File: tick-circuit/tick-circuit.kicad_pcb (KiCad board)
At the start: 2 copper layers, 48.3 x 33 mm, 14 parts, among them J1 Power, J2 50/60Hz, U1 74HCT4060, U2 74HCT73, X1 3.93216 MHz

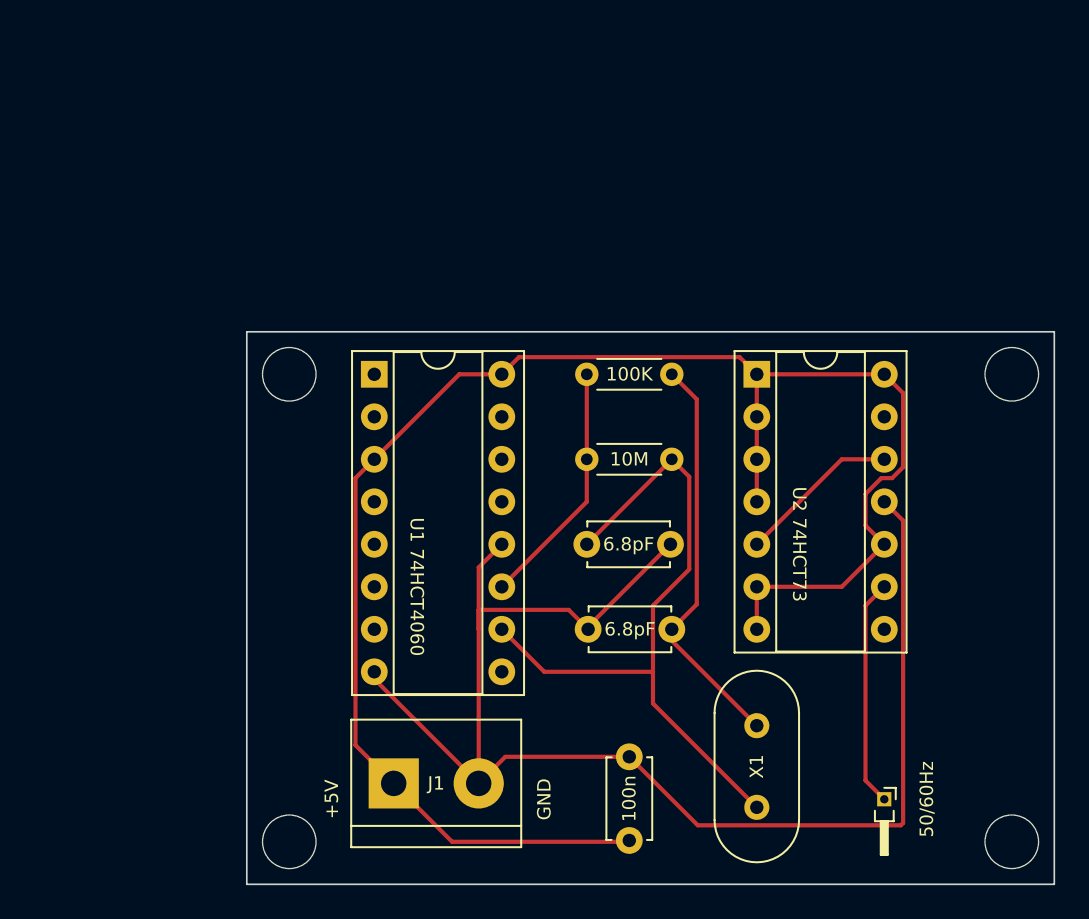
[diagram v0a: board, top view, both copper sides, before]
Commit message: Use both layers, add ground fills
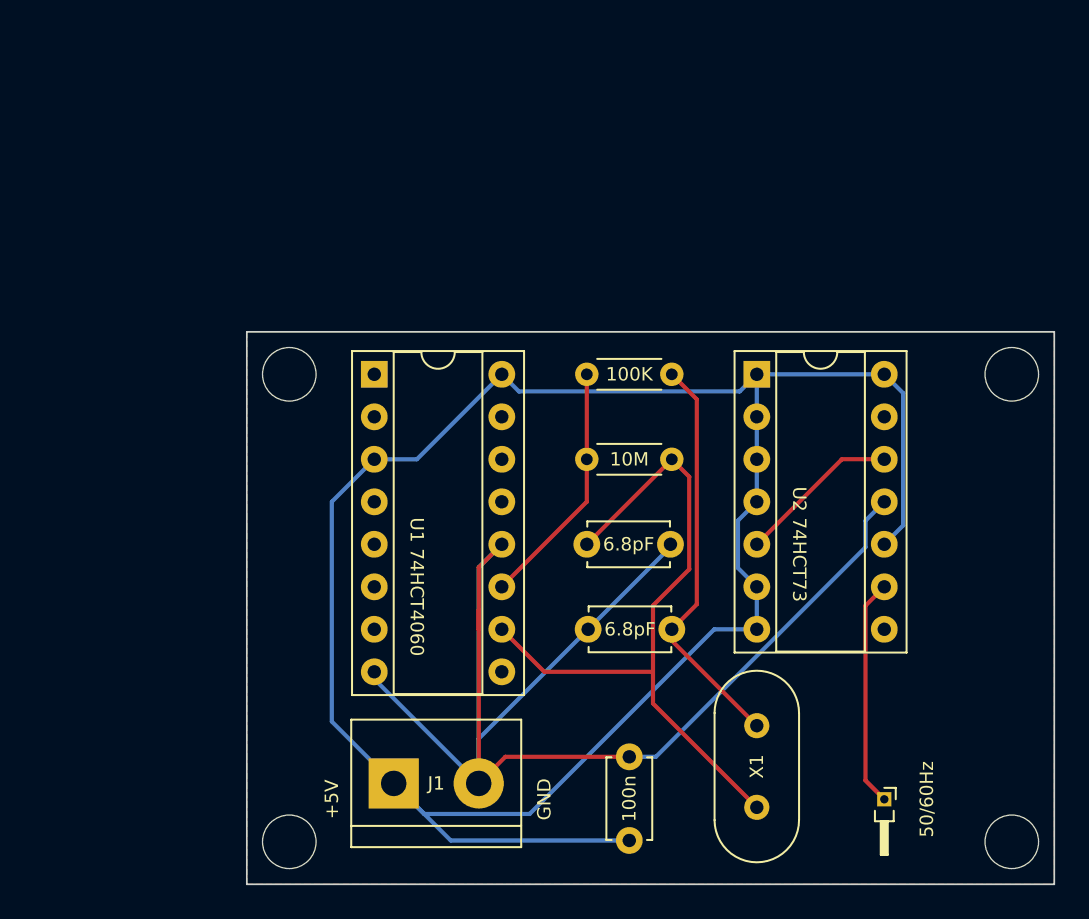
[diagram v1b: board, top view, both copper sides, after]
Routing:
- net +5V: track 101.0 -> 125.2 mm
- net GND: track 86.9 -> 91.3 mm
- added copper zone on B.Cu, net GND
- added copper zone on F.Cu, net GND
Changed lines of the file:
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@@
   (segment (start 50.8 38.1) (end 51.845 39.145) (width 0.25) (layer "F.Cu") (net 1))
   (segment (start 55.88 58.42) (end 55.88 58.9) (width 0.25) (layer "F.Cu") (net 1))
-  (segment (start 45.8 48.1) (end 45.8 48.26) (width 0.25) (layer "F.Cu") (net 2))
   (segment (start 39.26 47.1) (end 39.26 48.26) (width 0.25) (layer "F.Cu") (net 2))
-  (segment (start 33.02 51.23) (end 33.02 50.8) (width 0.25) (layer "F.Cu") (net 2))
   (segment (start 39.26 48.26) (end 39.26 44.56) (width 0.25) (layer "F.Cu") (net 2))
-  (segment (start 64.485 59.975) (end 52.355 59.975) (width 0.25) (layer "F.Cu") (net 2))
   (segment (start 39.26 57.47) (end 39.26 48.26) (width 0.25) (layer "F.Cu") (net 2))
-  (segment (start 63.5 40.64) (end 64.625 41.765) (width 0.25) (layer "F.Cu") (net 2))
   (segment (start 40.85 55.88) (end 39.26 57.47) (width 0.25) (layer "F.Cu") (net 2))
   (segment (start 48.26 55.88) (end 40.85 55.88) (width 0.25) (layer "F.Cu") (net 2))
-  (segment (start 44.64 47.1) (end 39.26 47.1) (width 0.25) (layer "F.Cu") (net 2))
-  (segment (start 50.72 43.18) (end 45.8 48.1) (width 0.25) (layer "F.Cu") (net 2))
   (segment (start 39.26 44.56) (end 40.64 43.18) (width 0.25) (layer "F.Cu") (net 2))
-  (segment (start 45.8 48.26) (end 44.64 47.1) (width 0.25) (layer "F.Cu") (net 2))
-  (segment (start 64.625 41.765) (end 64.625 59.835) (width 0.25) (layer "F.Cu") (net 2))
-  (segment (start 64.625 59.835) (end 64.485 59.975) (width 0.25) (layer "F.Cu") (net 2))
-  (segment (start 52.355 59.975) (end 48.26 55.88) (width 0.25) (layer "F.Cu") (net 2))
-  (segment (start 39.26 57.47) (end 33.02 51.23) (width 0.25) (layer "F.Cu") (net 2))
+  (segment (start 39.26 44.56) (end 40.64 43.18) (width 0.25) (layer "B.Cu") (net 2))
+  (segment (start 39.26 57.47) (end 39.26 44.56) (width 0.25) (layer "B.Cu") (net 2))
+  (segment (start 39.26 57.47) (end 33.02 51.23) (width 0.25) (layer "B.Cu") (net 2))
+  (segment (start 33.02 51.23) (end 33.02 50.8) (width 0.25) (layer "B.Cu") (net 2))
+  (segment (start 48.26 55.88) (end 49.850991 55.88) (width 0.25) (layer "B.Cu") (net 2))
+  (segment (start 49.850991 55.88) (end 62.375 43.355991) (width 0.25) (layer "B.Cu") (net 2))
+  (segment (start 39.26 54.8) (end 45.8 48.26) (width 0.25) (layer "B.Cu") (net 2))
+  (segment (start 45.8 48.26) (end 50.72 43.34) (width 0.25) (layer "B.Cu") (net 2))
+  (segment (start 62.375 41.765) (end 63.5 40.64) (width 0.25) (layer "B.Cu") (net 2))
+  (segment (start 62.375 43.355991) (end 62.375 41.765) (width 0.25) (layer "B.Cu") (net 2))
+  (segment (start 50.72 43.34) (end 50.72 43.18) (width 0.25) (layer "B.Cu") (net 2))
+  (segment (start 39.26 57.47) (end 39.26 54.8) (width 0.25) (layer "B.Cu") (net 2))
   (segment (start 55.88 54.02) (end 50.8 48.94) (width 0.25) (layer "F.Cu") (net 3))
   (segment (start 50.8 48.94) (end 50.8 48.26) (width 0.25) (layer "F.Cu") (net 3))
@@
   (segment (start 50.8 33.02) (end 52.295 34.515) (width 0.25) (layer "F.Cu") (net 3))
   (segment (start 52.295 34.515) (end 52.295 46.765) (width 0.25) (layer "F.Cu") (net 3))
-  (segment (start 34.18 57.47) (end 31.895 55.185) (width 0.25) (layer "F.Cu") (net 4))
-  (segment (start 31.895 55.185) (end 31.895 39.225) (width 0.25) (layer "F.Cu") (net 4))
-  (segment (start 55.88 33.02) (end 55.88 35.56) (width 0.25) (layer "F.Cu") (net 4))
-  (segment (start 34.18 57.47) (end 37.67 60.96) (width 0.25) (layer "F.Cu") (net 4))
-  (segment (start 31.895 39.225) (end 33.02 38.1) (width 0.25) (layer "F.Cu") (net 4))
-  (segment (start 62.375 40.174009) (end 63.324009 39.225) (width 0.25) (layer "F.Cu") (net 4))
-  (segment (start 63.324009 39.225) (end 63.965991 39.225) (width 0.25) (layer "F.Cu") (net 4))
-  (segment (start 38.1 33.02) (end 40.64 33.02) (width 0.25) (layer "F.Cu") (net 4))
-  (segment (start 55.88 35.56) (end 55.88 38.1) (width 0.25) (layer "F.Cu") (net 4))
-  (segment (start 63.965991 39.225) (end 64.625 38.565991) (width 0.25) (layer "F.Cu") (net 4))
-  (segment (start 55.88 33.02) (end 63.5 33.02) (width 0.25) (layer "F.Cu") (net 4))
-  (segment (start 37.67 60.96) (end 48.26 60.96) (width 0.25) (layer "F.Cu") (net 4))
-  (segment (start 33.02 38.1) (end 38.1 33.02) (width 0.25) (layer "F.Cu") (net 4))
-  (segment (start 60.96 45.72) (end 63.5 43.18) (width 0.25) (layer "F.Cu") (net 4))
-  (segment (start 55.88 45.72) (end 60.96 45.72) (width 0.25) (layer "F.Cu") (net 4))
-  (segment (start 54.855 31.995) (end 55.88 33.02) (width 0.25) (layer "F.Cu") (net 4))
-  (segment (start 64.625 38.565991) (end 64.625 34.145) (width 0.25) (layer "F.Cu") (net 4))
-  (segment (start 63.5 43.18) (end 62.375 42.055) (width 0.25) (layer "F.Cu") (net 4))
-  (segment (start 40.64 33.02) (end 41.665 31.995) (width 0.25) (layer "F.Cu") (net 4))
-  (segment (start 55.88 38.1) (end 55.88 40.64) (width 0.25) (layer "F.Cu") (net 4))
-  (segment (start 62.375 42.055) (end 62.375 40.174009) (width 0.25) (layer "F.Cu") (net 4))
-  (segment (start 41.665 31.995) (end 54.855 31.995) (width 0.25) (layer "F.Cu") (net 4))
-  (segment (start 63.5 33.02) (end 64.625 34.145) (width 0.25) (layer "F.Cu") (net 4))
-  (segment (start 55.88 45.72) (end 55.88 48.26) (width 0.25) (layer "F.Cu") (net 4))
+  (segment (start 37.59 60.88) (end 34.18 57.47) (width 0.25) (layer "B.Cu") (net 4))
+  (segment (start 63.5 43.18) (end 64.625 42.055) (width 0.25) (layer "B.Cu") (net 4))
+  (segment (start 54.855 34.045) (end 41.665 34.045) (width 0.25) (layer "B.Cu") (net 4))
+  (segment (start 33.02 38.1) (end 30.48 40.64) (width 0.25) (layer "B.Cu") (net 4))
+  (segment (start 64.625 34.145) (end 63.5 33.02) (width 0.25) (layer "B.Cu") (net 4))
+  (segment (start 30.48 40.64) (end 30.48 53.77) (width 0.25) (layer "B.Cu") (net 4))
+  (segment (start 54.755 41.765) (end 55.88 40.64) (width 0.25) (layer "B.Cu") (net 4))
+  (segment (start 48.26 60.88) (end 37.59 60.88) (width 0.25) (layer "B.Cu") (net 4))
+  (segment (start 55.88 33.02) (end 63.5 33.02) (width 0.25) (layer "B.Cu") (net 4))
+  (segment (start 55.88 33.02) (end 55.88 35.56) (width 0.25) (layer "B.Cu") (net 4))
+  (segment (start 30.48 53.77) (end 34.18 57.47) (width 0.25) (layer "B.Cu") (net 4))
+  (segment (start 55.88 38.1) (end 55.88 40.64) (width 0.25) (layer "B.Cu") (net 4))
+  (segment (start 33.02 38.1) (end 35.56 38.1) (width 0.25) (layer "B.Cu") (net 4))
+  (segment (start 41.665 34.045) (end 40.64 33.02) (width 0.25) (layer "B.Cu") (net 4))
+  (segment (start 53.34 48.26) (end 55.88 48.26) (width 0.25) (layer "B.Cu") (net 4))
+  (segment (start 36.005 59.295) (end 42.305 59.295) (width 0.25) (layer "B.Cu") (net 4))
+  (segment (start 54.755 44.595) (end 54.755 41.765) (width 0.25) (layer "B.Cu") (net 4))
+  (segment (start 55.88 35.56) (end 55.88 38.1) (width 0.25) (layer "B.Cu") (net 4))
+  (segment (start 35.56 38.1) (end 40.64 33.02) (width 0.25) (layer "B.Cu") (net 4))
+  (segment (start 55.88 33.02) (end 54.855 34.045) (width 0.25) (layer "B.Cu") (net 4))
+  (segment (start 55.88 45.72) (end 54.755 44.595) (width 0.25) (layer "B.Cu") (net 4))
+  (segment (start 55.88 48.26) (end 55.88 45.72) (width 0.25) (layer "B.Cu") (net 4))
+  (segment (start 34.18 57.47) (end 36.005 59.295) (width 0.25) (layer "B.Cu") (net 4))
+  (segment (start 42.305 59.295) (end 53.34 48.26) (width 0.25) (layer "B.Cu") (net 4))
+  (segment (start 64.625 42.055) (end 64.625 34.145) (width 0.25) (layer "B.Cu") (net 4))
   (segment (start 62.375 46.845) (end 63.5 45.72) (width 0.25) (layer "F.Cu") (net 5))
   (segment (start 62.375 57.295) (end 62.375 46.845) (width 0.25) (layer "F.Cu") (net 5))
@@
   (segment (start 60.96 38.1) (end 55.88 43.18) (width 0.25) (layer "F.Cu") (net 17))
   (segment (start 63.5 38.1) (end 60.96 38.1) (width 0.25) (layer "F.Cu") (net 17))
+  (zone (net 2) (net_name "GND") (layer "F.Cu") (hatch edge 0.5)
+    (connect_pads (clearance 0.5))
+    (min_thickness 0.25) (filled_areas_thickness no)
+    (fill yes (thermal_gap 0.5) (thermal_bridge_width 0.5))
+    (polygon
+      (pts
+        (xy 25.4 30.48)
+        (xy 25.4 63.5)
+        (xy 73.66 63.5)
+        (xy 73.66 30.48)
+      )
+    )
+  )
+  (zone (net 2) (net_name "GND") (layer "B.Cu") (hatch edge 0.5)
+    (priority 1)
+    (connect_pads (clearance 0.5))
+    (min_thickness 0.25) (filled_areas_thickness no)
+    (fill yes (thermal_gap 0.5) (thermal_bridge_width 0.5))
+    (polygon
+      (pts
+        (xy 25.4 30.48)
+        (xy 73.66 30.48)
+        (xy 73.66 63.5)
+        (xy 25.4 63.5)
+      )
+    )
+  )
 )

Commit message: No need for ground routing if it is all ground
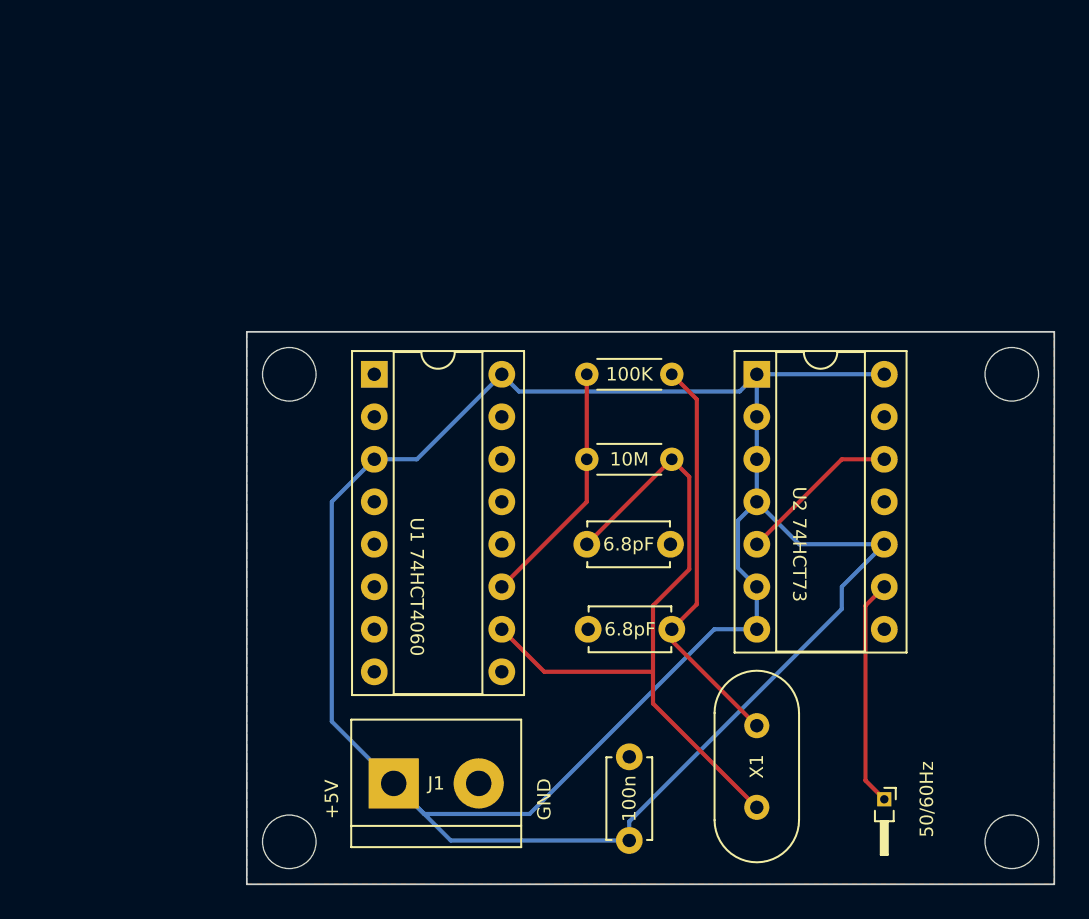
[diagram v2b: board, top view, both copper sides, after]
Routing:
- net GND: track 91.3 -> 0.59 mm
- net +5V: track 125.2 -> 146.8 mm
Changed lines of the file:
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@@
   (segment (start 50.8 38.1) (end 51.845 39.145) (width 0.25) (layer "F.Cu") (net 1))
   (segment (start 55.88 58.42) (end 55.88 58.9) (width 0.25) (layer "F.Cu") (net 1))
-  (segment (start 39.26 47.1) (end 39.26 48.26) (width 0.25) (layer "F.Cu") (net 2))
-  (segment (start 39.26 48.26) (end 39.26 44.56) (width 0.25) (layer "F.Cu") (net 2))
-  (segment (start 39.26 57.47) (end 39.26 48.26) (width 0.25) (layer "F.Cu") (net 2))
-  (segment (start 40.85 55.88) (end 39.26 57.47) (width 0.25) (layer "F.Cu") (net 2))
-  (segment (start 48.26 55.88) (end 40.85 55.88) (width 0.25) (layer "F.Cu") (net 2))
-  (segment (start 39.26 44.56) (end 40.64 43.18) (width 0.25) (layer "F.Cu") (net 2))
-  (segment (start 39.26 44.56) (end 40.64 43.18) (width 0.25) (layer "B.Cu") (net 2))
-  (segment (start 39.26 57.47) (end 39.26 44.56) (width 0.25) (layer "B.Cu") (net 2))
-  (segment (start 39.26 57.47) (end 33.02 51.23) (width 0.25) (layer "B.Cu") (net 2))
   (segment (start 33.02 51.23) (end 33.02 50.8) (width 0.25) (layer "B.Cu") (net 2))
-  (segment (start 48.26 55.88) (end 49.850991 55.88) (width 0.25) (layer "B.Cu") (net 2))
-  (segment (start 49.850991 55.88) (end 62.375 43.355991) (width 0.25) (layer "B.Cu") (net 2))
-  (segment (start 39.26 54.8) (end 45.8 48.26) (width 0.25) (layer "B.Cu") (net 2))
-  (segment (start 45.8 48.26) (end 50.72 43.34) (width 0.25) (layer "B.Cu") (net 2))
-  (segment (start 62.375 41.765) (end 63.5 40.64) (width 0.25) (layer "B.Cu") (net 2))
-  (segment (start 62.375 43.355991) (end 62.375 41.765) (width 0.25) (layer "B.Cu") (net 2))
   (segment (start 50.72 43.34) (end 50.72 43.18) (width 0.25) (layer "B.Cu") (net 2))
-  (segment (start 39.26 57.47) (end 39.26 54.8) (width 0.25) (layer "B.Cu") (net 2))
   (segment (start 55.88 54.02) (end 50.8 48.94) (width 0.25) (layer "F.Cu") (net 3))
   (segment (start 50.8 48.94) (end 50.8 48.26) (width 0.25) (layer "F.Cu") (net 3))
@@
   (segment (start 50.8 33.02) (end 52.295 34.515) (width 0.25) (layer "F.Cu") (net 3))
   (segment (start 52.295 34.515) (end 52.295 46.765) (width 0.25) (layer "F.Cu") (net 3))
+  (segment (start 60.96 47.04863) (end 60.96 45.72) (width 0.25) (layer "B.Cu") (net 4))
   (segment (start 37.59 60.88) (end 34.18 57.47) (width 0.25) (layer "B.Cu") (net 4))
-  (segment (start 63.5 43.18) (end 64.625 42.055) (width 0.25) (layer "B.Cu") (net 4))
+  (segment (start 58.42 43.18) (end 55.88 40.64) (width 0.25) (layer "B.Cu") (net 4))
+  (segment (start 63.5 43.18) (end 58.42 43.18) (width 0.25) (layer "B.Cu") (net 4))
   (segment (start 54.855 34.045) (end 41.665 34.045) (width 0.25) (layer "B.Cu") (net 4))
   (segment (start 33.02 38.1) (end 30.48 40.64) (width 0.25) (layer "B.Cu") (net 4))
-  (segment (start 64.625 34.145) (end 63.5 33.02) (width 0.25) (layer "B.Cu") (net 4))
   (segment (start 30.48 40.64) (end 30.48 53.77) (width 0.25) (layer "B.Cu") (net 4))
   (segment (start 54.755 41.765) (end 55.88 40.64) (width 0.25) (layer "B.Cu") (net 4))
   (segment (start 48.26 60.88) (end 37.59 60.88) (width 0.25) (layer "B.Cu") (net 4))
   (segment (start 55.88 33.02) (end 63.5 33.02) (width 0.25) (layer "B.Cu") (net 4))
+  (segment (start 48.26 60.88) (end 48.26 59.74863) (width 0.25) (layer "B.Cu") (net 4))
   (segment (start 55.88 33.02) (end 55.88 35.56) (width 0.25) (layer "B.Cu") (net 4))
   (segment (start 30.48 53.77) (end 34.18 57.47) (width 0.25) (layer "B.Cu") (net 4))
+  (segment (start 60.96 45.72) (end 63.5 43.18) (width 0.25) (layer "B.Cu") (net 4))
   (segment (start 55.88 38.1) (end 55.88 40.64) (width 0.25) (layer "B.Cu") (net 4))
   (segment (start 33.02 38.1) (end 35.56 38.1) (width 0.25) (layer "B.Cu") (net 4))
@@
   (segment (start 53.34 48.26) (end 55.88 48.26) (width 0.25) (layer "B.Cu") (net 4))
   (segment (start 36.005 59.295) (end 42.305 59.295) (width 0.25) (layer "B.Cu") (net 4))
+  (segment (start 48.26 59.74863) (end 60.96 47.04863) (width 0.25) (layer "B.Cu") (net 4))
   (segment (start 54.755 44.595) (end 54.755 41.765) (width 0.25) (layer "B.Cu") (net 4))
   (segment (start 55.88 35.56) (end 55.88 38.1) (width 0.25) (layer "B.Cu") (net 4))
@@
   (segment (start 34.18 57.47) (end 36.005 59.295) (width 0.25) (layer "B.Cu") (net 4))
   (segment (start 42.305 59.295) (end 53.34 48.26) (width 0.25) (layer "B.Cu") (net 4))
-  (segment (start 64.625 42.055) (end 64.625 34.145) (width 0.25) (layer "B.Cu") (net 4))
   (segment (start 62.375 46.845) (end 63.5 45.72) (width 0.25) (layer "F.Cu") (net 5))
   (segment (start 62.375 57.295) (end 62.375 46.845) (width 0.25) (layer "F.Cu") (net 5))

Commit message: Board was uneven
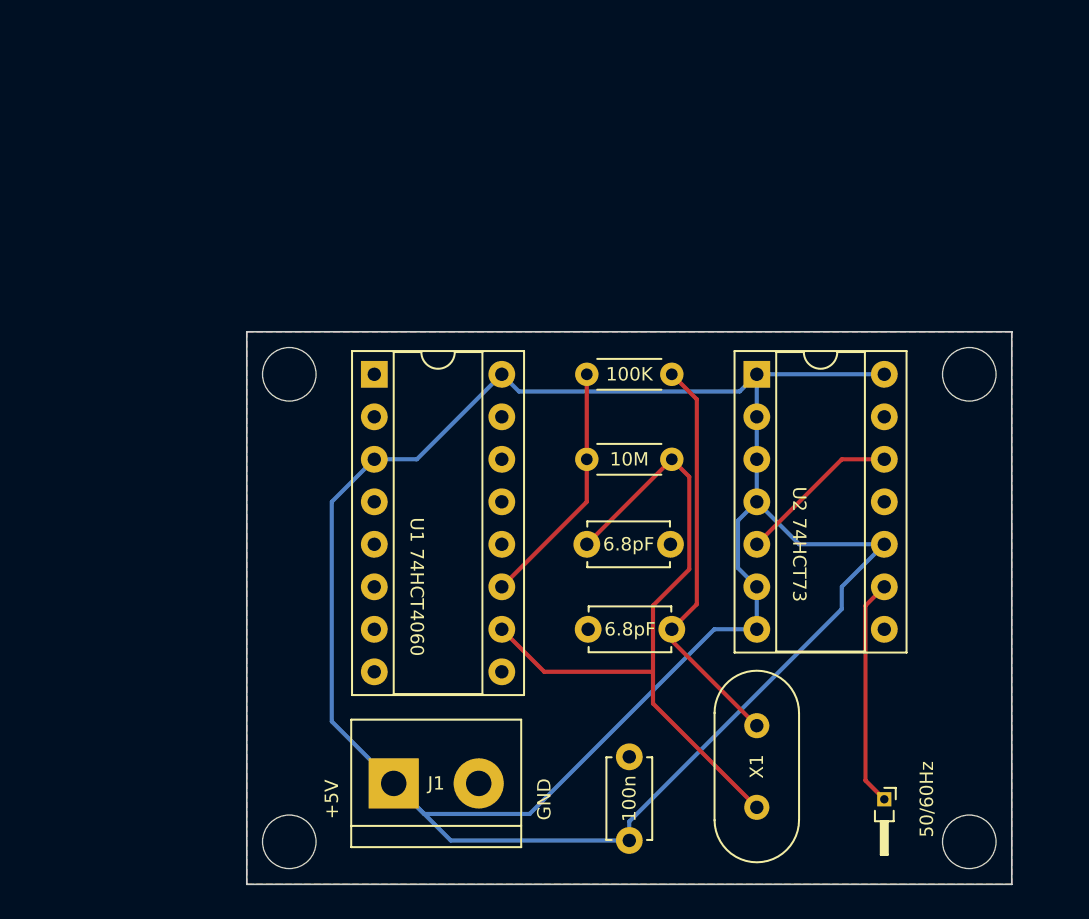
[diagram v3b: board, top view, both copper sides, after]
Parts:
- moved REF** 2.54 mm to (68.6, 61.0)
- moved REF** 2.54 mm to (68.6, 33.0)
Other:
- board size 48.3 x 33 mm -> 45.7 x 33 mm
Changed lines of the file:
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@@
   )
   (footprint "MountingHole:MountingHole_3.2mm_M3" (layer "F.Cu")
-    (at 71.12 60.96)
+    (at 68.58 60.96)
     (descr "Mounting Hole 3.2mm, no annular, M3")
     (tags "mounting hole 3.2mm no annular m3")
@@
   )
   (footprint "MountingHole:MountingHole_3.2mm_M3" (layer "F.Cu")
-    (at 71.12 33.02)
+    (at 68.58 33.02)
     (descr "Mounting Hole 3.2mm, no annular, M3")
     (tags "mounting hole 3.2mm no annular m3")
@@
     )
   )
-  (gr_rect (start 25.4 30.48) (end 73.66 63.5)
+  (gr_rect (start 25.4 30.48) (end 71.12 63.5)
     (stroke (width 0.1) (type default)) (fill none) (layer "Edge.Cuts"))
   (gr_text "GND" (at 43.18 58.42 90) (layer "F.SilkS")
@@
         (xy 25.4 30.48)
         (xy 25.4 63.5)
-        (xy 73.66 63.5)
-        (xy 73.66 30.48)
+        (xy 71.12 63.5)
+        (xy 71.12 30.48)
       )
     )
@@
       (pts
         (xy 25.4 30.48)
-        (xy 73.66 30.48)
-        (xy 73.66 63.5)
+        (xy 71.12 30.48)
+        (xy 71.12 63.5)
         (xy 25.4 63.5)
       )
